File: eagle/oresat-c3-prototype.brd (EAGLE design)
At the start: 99.8 x 94.7 mm, 106 parts, among them J1 J-SAMTEC-TFM-110-X1-XXX-D-RA, J2 U.FL, J3 U.FL, J4 U.FL, J6 J-SAMTEC-TFM-120-X1-XXX-D-RA, J7 FTSH-105-XX-X-DV-K, J8 SD_CARD_SOCKET, Q1 MOSFET-PCH-SOT23-6, Q3 MOSFET-PCH-SOT23-6, Q4 MOSFET-PCH-SOT23-6, Q5 PMV45EN, Q6 PMV45EN, U1 MAX4211CETE, U2 TCAN330, U3 TCAN330, U4 MAX4211CETE, U5 TPS62111RSA, U6 MAX6374KA+21-0078H-L, X1 16MHZ-2.5x2mm

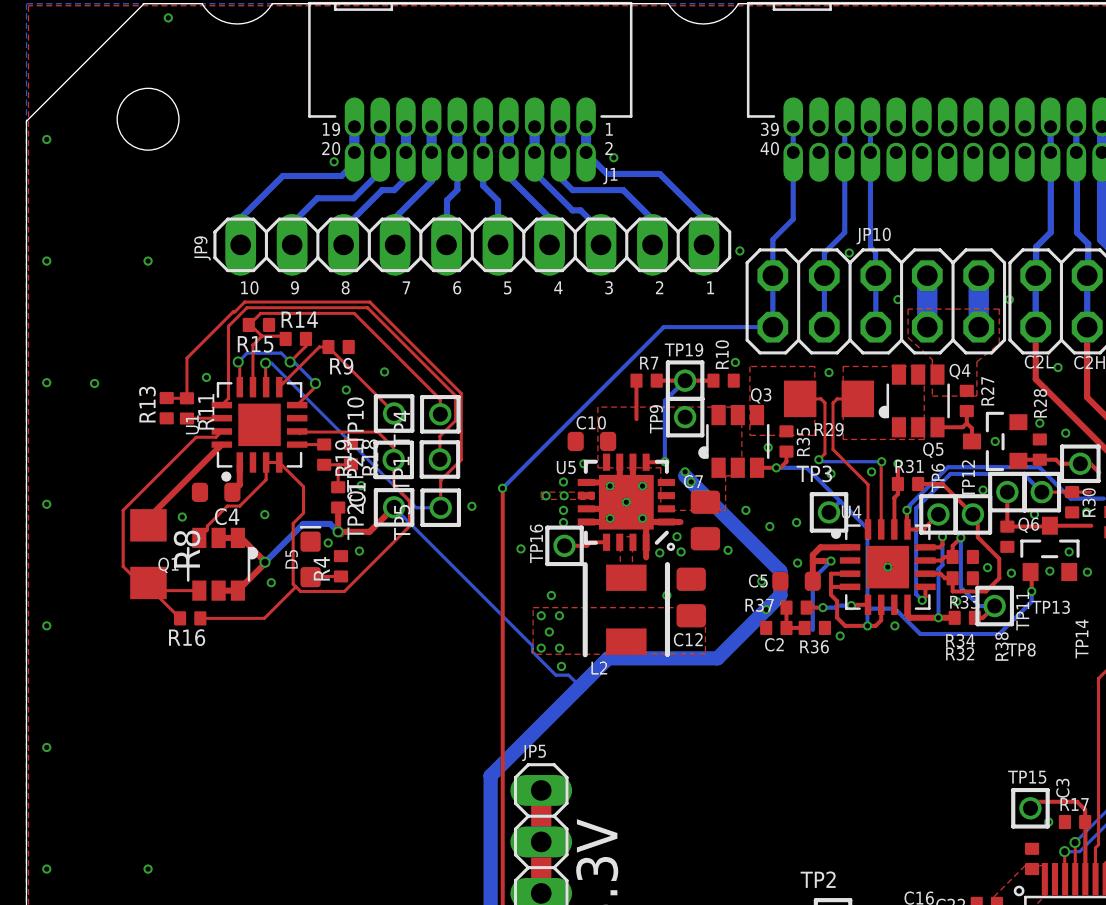
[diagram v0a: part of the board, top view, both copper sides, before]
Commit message: Added the circuit breaker schematic and wired it to the board part tps25961
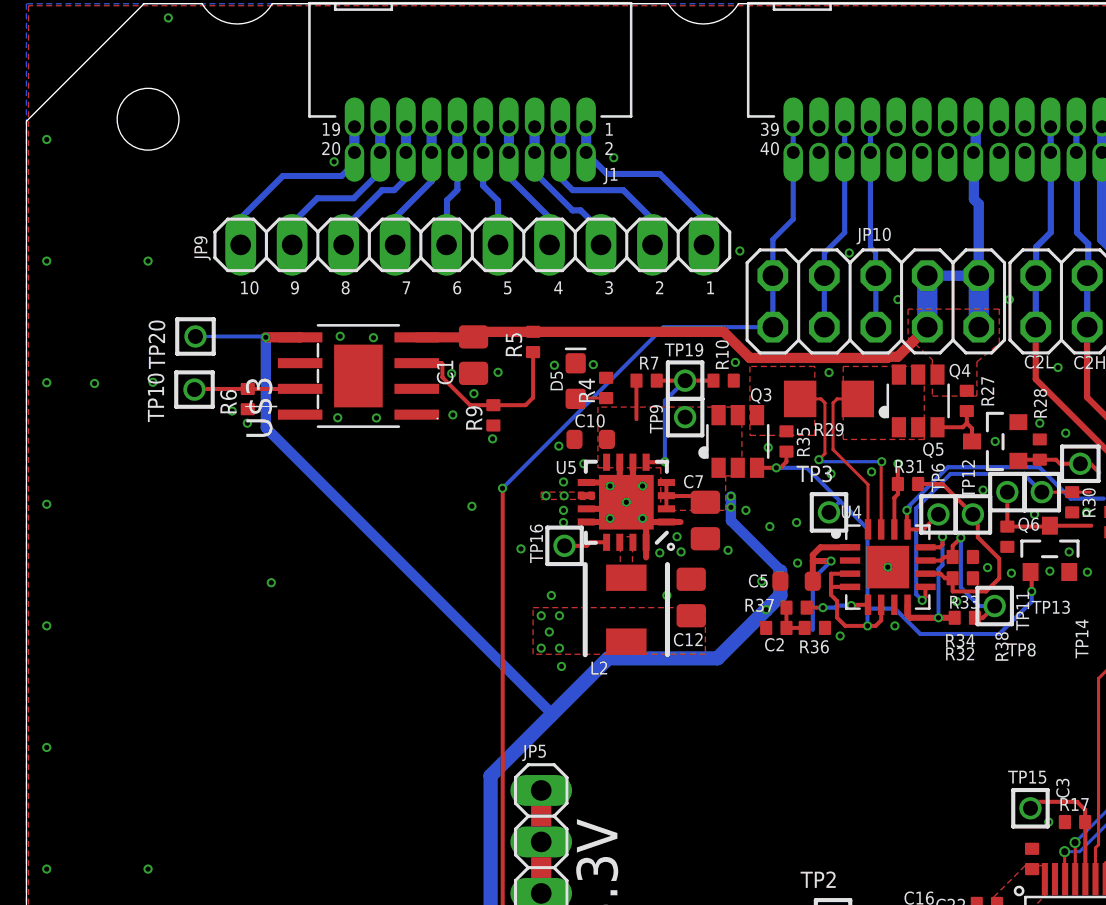
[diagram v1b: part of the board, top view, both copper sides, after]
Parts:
- removed C4: 1u, oresat-rcl:.0603-B-NOSILK
- removed Q1: MOSFET-PCH-SOT23-6, Q-MOSFET-PCH-SOT23-6:SOT23-6
- removed R11, R14: 0, rcl_custom:.0402-B-NOSILK
- removed R13, R15, R18, R19: NP, rcl_custom:.0402-B-NOSILK
- removed R16: 10k, rcl_custom:.0402-B-NOSILK
- removed R8: 100m, rcl:R1206
- removed TP1, TP21, TP4, TP5: TEST-POINT, Tova:2MM-TEST-POINT
- removed U1: MAX4211CETE, U-Maxim-MAX4211-power-monitor:QFN65P400X400X80-17T210
- added R5: 10k, rcl_custom:.0402-B-NOSILK
- added R6: 4.7k, rcl_custom:.0402-B-NOSILK
- added U$3: TI-TPS259621-eFuse, Robins_Parts:SO-POWERPAD-8
- C1: value NP -> 1u; device rcl_custom:.0402-B-NOSILK -> oresat-rcl:.0805-B-NOSILK
- moved D5 15.8 mm to (27.1, 76.1)
- moved R4 15.8 mm to (28.6, 75.7)
- moved TP20 12.9 mm to (8.34, 78.3)
- moved TP10 9.92 mm to (8.29, 75.7)
- moved C1 9.69 mm to (22.1, 77.4), turned to 90 degrees
- moved R9 8.35 mm to (23.0, 74.4), turned to 90 degrees
- moved C10 0.12 mm to (27.8, 73.2)
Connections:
- removed net CB_POUT: TP1.1, U1.13
- removed net IOUT1: R11.2, U1.14
- removed net N$402: R9.2, TP10.1, U1.9
- removed net N$403: R11.1, R13.2, TP5.1, U1.10
- removed net N$404: R14.1, R15.2, TP4.1, U1.11
- removed net N$405: R14.2, U1.12, U1.8
- removed net N$407: R19.1, U1.5
- removed net N$479: C1.1, R18.2, R19.2
- removed net N$480: Q1.4, R16.2, R8.2, U1.15
- new net EN/UVLO: R5.1, R9.2, U$3.3
- new net ILIM: R6.2, TP10.1, U$3.7
- net 3.3V: no longer C4.1, U1.1
- net CB_CTRL: no longer Q1.3, R16.1, TP21.1, U1.3, U1.4, U1.6
- net GND: now also C1.1, R6.1, U$3.1, U$3.THERMAL; no longer C4.2, R13.1, R15.1, R18.1, U1.7, U1.EPAD
- net VBUS: now also C1.2, R5.2, U$3.4; no longer R8.1, U1.16
- net VBUSP: now also U$3.5; no longer C1.2, Q1.1, Q1.2, Q1.5, Q1.6
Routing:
- net N$403: track 38.4 -> 0.00 mm, vias 1 -> 0
- net CB_CTRL: track 66.4 -> 31.6 mm
- net VBUS: track 10.6 -> 41.6 mm
- net CB_POUT: track 20.9 -> 0.00 mm
- net N$404: track 17.4 -> 0.00 mm
- net N$480: track 15.5 -> 0.00 mm
- net EN/UVLO: track 0.00 -> 9.40 mm
- net N$405: track 9.04 -> 0.00 mm, vias 3 -> 0
- net N$402: track 7.87 -> 0.00 mm
- net ILIM: track 0.00 -> 5.19 mm
- net N$479: track 2.44 -> 0.00 mm
- net VBUSP: track 100.1 -> 102.5 mm, vias 5 -> 4
- net IOUT1: track 1.73 -> 0.00 mm
- net 3.3V: track 109.7 -> 108.1 mm
- net N$407: track 1.33 -> 0.00 mm
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
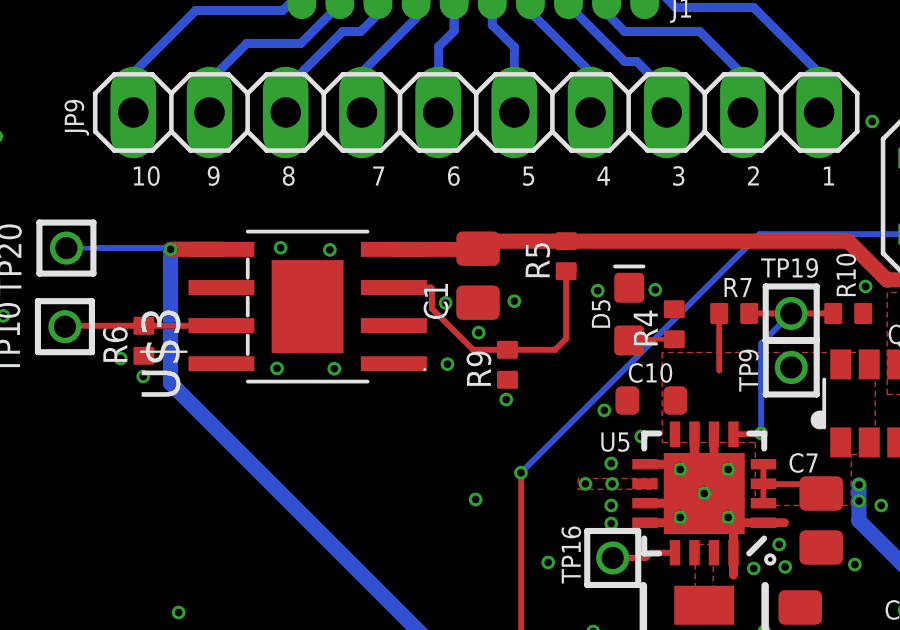
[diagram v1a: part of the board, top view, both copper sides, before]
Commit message: I corrected R_ILIM on the CB to set the over current limit to 0.302 A.
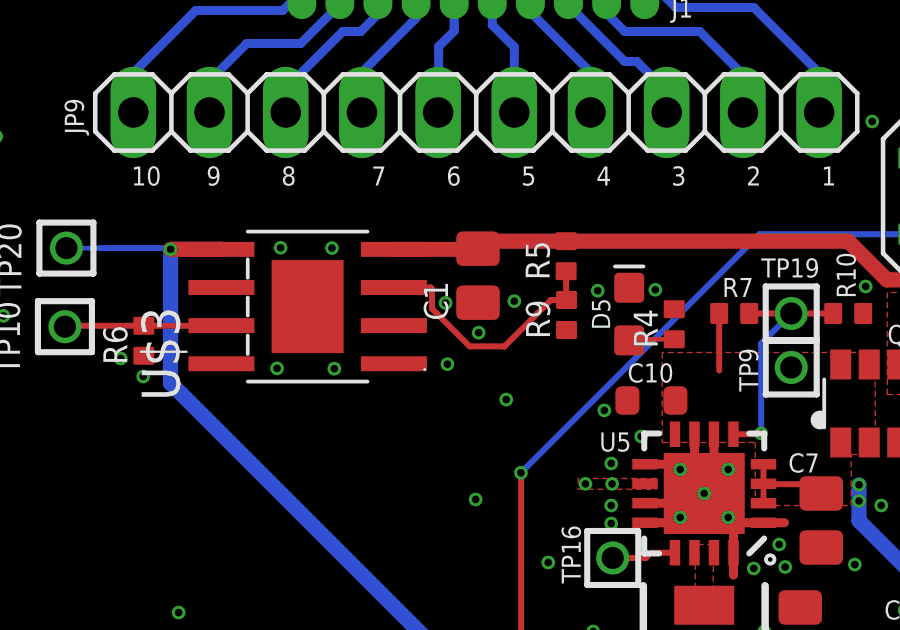
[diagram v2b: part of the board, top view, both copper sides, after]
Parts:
- R6: value 4.7k -> 3.1k
- moved R9 2.58 mm to (25.0, 76.0)
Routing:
- net EN/UVLO: track 9.40 -> 8.57 mm
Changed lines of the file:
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@@
 <attribute name="VALUE" x="29.95" y="74.94" size="0.8" layer="27" font="vector" ratio="15" rot="R90"/>
 </element>
-<element name="R9" library="rcl_custom" package=".0402-B-NOSILK" value="10k" x="23.04" y="74.39" smashed="yes" rot="R90">
-<attribute name="DIS" value="Digi-Key" x="17.74" y="68.49" size="1.778" layer="27" rot="R90" display="off"/>
-<attribute name="DPN" value="1276-4275-1-ND" x="17.74" y="68.49" size="1.778" layer="27" rot="R90" display="off"/>
-<attribute name="MFR" value="Samsung" x="17.74" y="68.49" size="1.778" layer="27" rot="R90" display="off"/>
-<attribute name="MPN" value="RC1005F6653CS" x="17.74" y="68.49" size="1.778" layer="27" rot="R90" display="off"/>
-<attribute name="NAME" x="22.49" y="73.59" size="0.8" layer="25" font="vector" ratio="15" rot="R90"/>
-<attribute name="NAME" x="23.04" y="74.39" size="0.2" layer="33" ratio="15" rot="R90" align="center"/>
-<attribute name="VALUE" x="24.39" y="73.59" size="0.8" layer="27" font="vector" ratio="15" rot="R90"/>
+<element name="R9" library="rcl_custom" package=".0402-B-NOSILK" value="10k" x="25.01" y="76.05" smashed="yes" rot="R90">
+<attribute name="DIS" value="Digi-Key" x="19.71" y="70.15" size="1.778" layer="27" rot="R90" display="off"/>
+<attribute name="DPN" value="1276-4275-1-ND" x="19.71" y="70.15" size="1.778" layer="27" rot="R90" display="off"/>
+<attribute name="MFR" value="Samsung" x="19.71" y="70.15" size="1.778" layer="27" rot="R90" display="off"/>
+<attribute name="MPN" value="RC1005F6653CS" x="19.71" y="70.15" size="1.778" layer="27" rot="R90" display="off"/>
+<attribute name="NAME" x="24.46" y="75.25" size="0.8" layer="25" font="vector" ratio="15" rot="R90"/>
+<attribute name="NAME" x="25.01" y="76.05" size="0.2" layer="33" ratio="15" rot="R90" align="center"/>
+<attribute name="VALUE" x="26.36" y="75.25" size="0.8" layer="27" font="vector" ratio="15" rot="R90"/>
 </element>
 <element name="TP10" library="Tova" package="2MM-TEST-POINT" value="TEST-POINT" x="8.29" y="75.66" smashed="yes" rot="R90">
@@
 <attribute name="VALUE" x="23.86" y="75.86" size="0.8" layer="27" font="vector" ratio="15" rot="R90"/>
 </element>
-<element name="R6" library="rcl_custom" package=".0402-B-NOSILK" value="4.7k" x="10.92" y="75.19" smashed="yes" rot="R90">
+<element name="R6" library="rcl_custom" package=".0402-B-NOSILK" value="3.1k" x="10.92" y="75.19" smashed="yes" rot="R90">
 <attribute name="DIS" value="Digi-Key" x="10.92" y="75.19" size="1.778" layer="27" rot="R90" display="off"/>
 <attribute name="DPN" value="1276-4275-1-ND" x="10.92" y="75.19" size="1.778" layer="27" rot="R90" display="off"/>
@@
 <via x="17.27" y="74.26" extent="1-16" drill="0.254"/>
 <via x="15.48" y="78.29" extent="1-16" drill="0.254"/>
-<via x="17.12" y="78.22" extent="1-16" drill="0.254"/>
+<via x="17.19" y="78.28" extent="1-16" drill="0.254"/>
 <wire x1="98.8" y1="88" x2="93" y2="94" width="0" layer="19" extent="1-1"/>
 <wire x1="98.8" y1="82" x2="98.8" y2="88" width="0" layer="19" extent="1-1"/>
@@
 <wire x1="36.6" y1="72.8" x2="35.5" y2="69.7" width="0" layer="19" extent="1-1"/>
 <wire x1="23" y1="73.23" x2="26.27" y2="72.87" width="0" layer="19" extent="1-1"/>
-<wire x1="23.04" y1="73.89" x2="23" y2="73.23" width="0" layer="19" extent="1-1"/>
-<wire x1="22.08" y1="75.46" x2="23.04" y2="73.89" width="0" layer="19" extent="1-1"/>
+<wire x1="25.01" y1="75.55" x2="23" y2="73.23" width="0" layer="19" extent="1-1"/>
+<wire x1="22.08" y1="75.46" x2="25.01" y2="75.55" width="0" layer="19" extent="1-1"/>
 <wire x1="22.06" y1="76.46" x2="22.08" y2="75.46" width="0" layer="19" extent="1-1"/>
 <wire x1="20.98" y1="76.45" x2="22.06" y2="76.46" width="0" layer="19" extent="1-1"/>
@@
 <wire x1="15.36" y1="74.27" x2="17.27" y2="74.26" width="0" layer="19" extent="1-1"/>
 <wire x1="16.38" y1="76.33" x2="17.27" y2="74.26" width="0" layer="19" extent="1-1"/>
-<wire x1="17.12" y1="78.22" x2="16.38" y2="76.33" width="0" layer="19" extent="1-1"/>
-<wire x1="15.48" y1="78.29" x2="17.12" y2="78.22" width="0" layer="19" extent="1-1"/>
+<wire x1="17.19" y1="78.28" x2="16.38" y2="76.33" width="0" layer="19" extent="1-1"/>
+<wire x1="15.48" y1="78.29" x2="17.19" y2="78.28" width="0" layer="19" extent="1-1"/>
 <wire x1="26.05" y1="76.86" x2="23.27" y2="76.51" width="0" layer="19" extent="1-1"/>
 <wire x1="27.1" y1="76.957" x2="26.05" y2="76.86" width="0" layer="19" extent="1-1"/>
@@
 <contactref element="R5" pad="1"/>
 <contactref element="U$3" pad="3"/>
-<wire x1="20.5244" y1="76.26128125" x2="20.5244" y2="76.9256" width="0.2" layer="1"/>
-<wire x1="23.04" y1="74.89" x2="21.89568125" y2="74.89" width="0.2" layer="1"/>
-<wire x1="21.89568125" y1="74.89" x2="20.5244" y2="76.26128125" width="0.2" layer="1"/>
-<wire x1="20.485" y1="76.965" x2="19.255" y2="76.965" width="0.2" layer="1"/>
-<wire x1="20.5244" y1="76.9256" x2="20.485" y2="76.965" width="0.2" layer="1"/>
-<wire x1="23.04" y1="74.89" x2="24.63" y2="74.89" width="0.2" layer="1"/>
-<wire x1="24.63" y1="74.89" x2="24.998253125" y2="75.258253125" width="0.2" layer="1"/>
-<wire x1="24.998253125" y1="75.258253125" x2="24.998253125" y2="77.51" width="0.2" layer="1"/>
+<wire x1="24.49" y1="76.55" x2="25.01" y2="76.55" width="0.2" layer="1"/>
+<wire x1="19.255" y1="76.965" x2="20.485" y2="76.965" width="0.2" layer="1"/>
+<wire x1="25.01" y1="76.55" x2="24.998253125" y2="76.55" width="0.2" layer="1"/>
+<wire x1="24.998253125" y1="76.55" x2="24.998253125" y2="77.51" width="0.2" layer="1"/>
+<wire x1="22.9356" y1="75.0044" x2="22.94" y2="75" width="0.2" layer="1"/>
+<wire x1="20.5244" y1="76.26128125" x2="21.78128125" y2="75.0044" width="0.2" layer="1"/>
+<wire x1="21.78128125" y1="75.0044" x2="22.9356" y2="75.0044" width="0.2" layer="1"/>
+<wire x1="20.485" y1="76.965" x2="20.5244" y2="76.9256" width="0.2" layer="1"/>
+<wire x1="20.5244" y1="76.9256" x2="20.5244" y2="76.26128125" width="0.2" layer="1"/>
+<wire x1="22.94" y1="75" x2="24.49" y2="76.55" width="0.2" layer="1"/>
 </signal>
 <signal name="ILIM">

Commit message: layed out most of the board awaiting review and adding BOM
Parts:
- added Q1: MOSFET-PCH-SOT23-6, Q-MOSFET-PCH-SOT23-6:SOT23-6
- added R11, R13, R8: 4.7k, rcl:R0402
- U6: value MAX6374KA+21-0078H-L -> MAX6373KA+21-0078H-L
- moved C9 26.5 mm to (46.6, 44.1), turned to 270 degrees
- moved TP15 2.54 mm to (48.7, 57.4)
- moved R17 1.32 mm to (51.8, 55.6)
- moved C5 0.35 mm to (38.0, 66.5)
- moved U6 0.11 mm to (38.1, 44.0)
- moved R38 0.07 mm to (48.4, 68.5)
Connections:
- removed net SDIO_CK: J8.5, U$2.53
- removed net SDIO_CMD: J8.2, U$2.54
- removed net SDIO_D0: J8.7, U$2.39
- removed net SDIO_D1: J8.8, U$2.40
- removed net SDIO_D2: J8.9, U$2.51
- removed net SDIO_D3: J8.1, U$2.52
- new net MMC_CS: J8.1, U$2.40
- new net N$6: J8.4, Q1.1, Q1.2, Q1.5, Q1.6
- new net SD_PWR_CYC: Q1.3
- new net SPI3_MISO: J8.7, U$2.52
- new net SPI3_MOSI: J8.2, U$2.53
- new net SPI3_SCK: J8.5, U$2.51
- net !SD: now also R13.2
- net 3.3V: now also Q1.4, R11.1, R13.1, R8.1; no longer J8.4
- net OPD_SCL: now also R8.2
- net OPD_SDA: now also R11.2
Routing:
- net 3.3V: track 108.1 -> 203.4 mm, vias 10 -> 15
- net OPD_ON/!OFF: track 4.28 -> 47.7 mm, vias 0 -> 2
- net OPD_PWR: track 10.6 -> 53.7 mm, vias 0 -> 1
- net CAN1_H: track 10.7 -> 48.9 mm
- net CAN1_L: track 10.7 -> 47.2 mm
- net OPD_!FAULT: track 5.86 -> 42.2 mm, vias 0 -> 2
- net OPD_CB_RESET: track 15.1 -> 51.2 mm, vias 1 -> 2
- net OPD_POUT_IN: track 0.00 -> 31.8 mm, vias 0 -> 2
- net SPI3_MOSI: track 0.00 -> 30.7 mm, vias 0 -> 2
- net PA15: track 3.31 -> 34.0 mm, vias 1 -> 2
- net SPI3_MISO: track 0.00 -> 29.3 mm, vias 0 -> 2
- net SPI3_SCK: track 0.00 -> 24.1 mm, vias 0 -> 2
- net MMC_CS: track 0.00 -> 22.6 mm
- net NRST: track 67.0 -> 78.2 mm
- net OPD_SDA: track 39.3 -> 48.4 mm
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
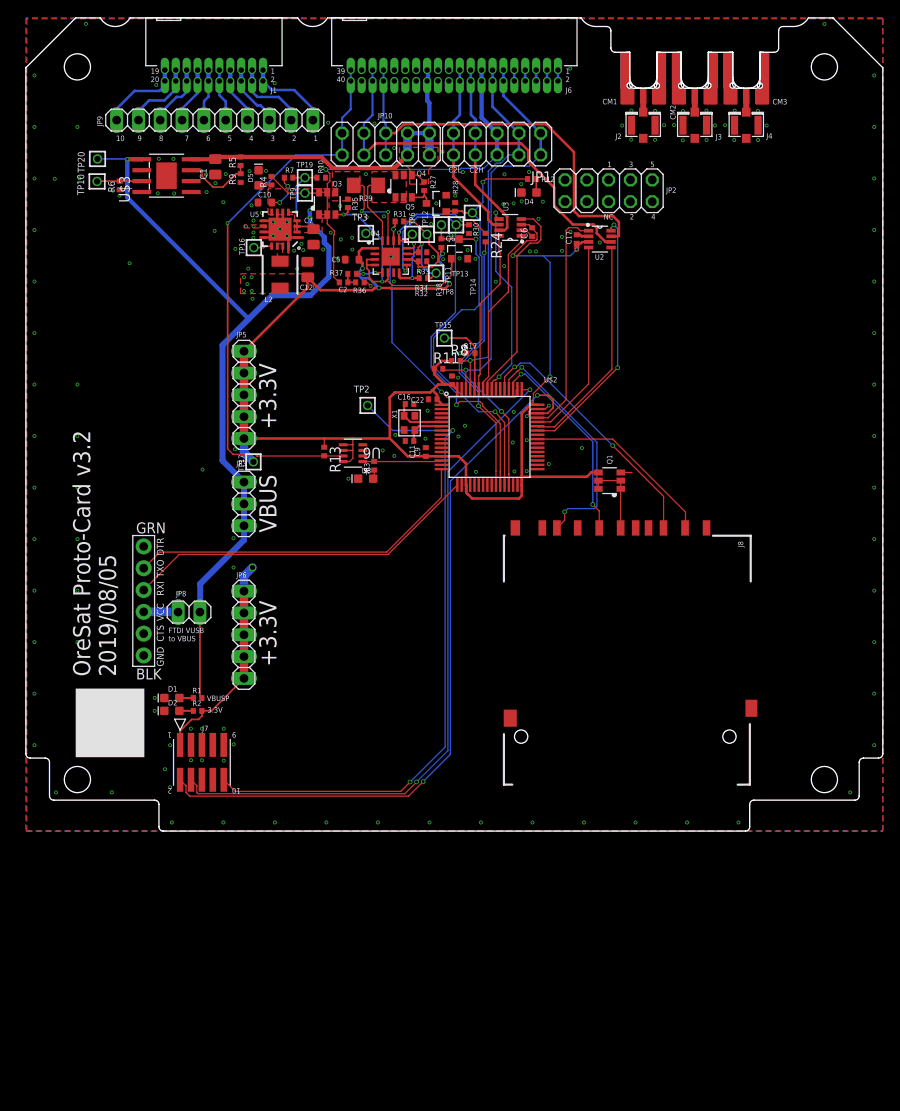
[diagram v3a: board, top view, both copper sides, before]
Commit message: Routed spare pins to header and a little cleanup
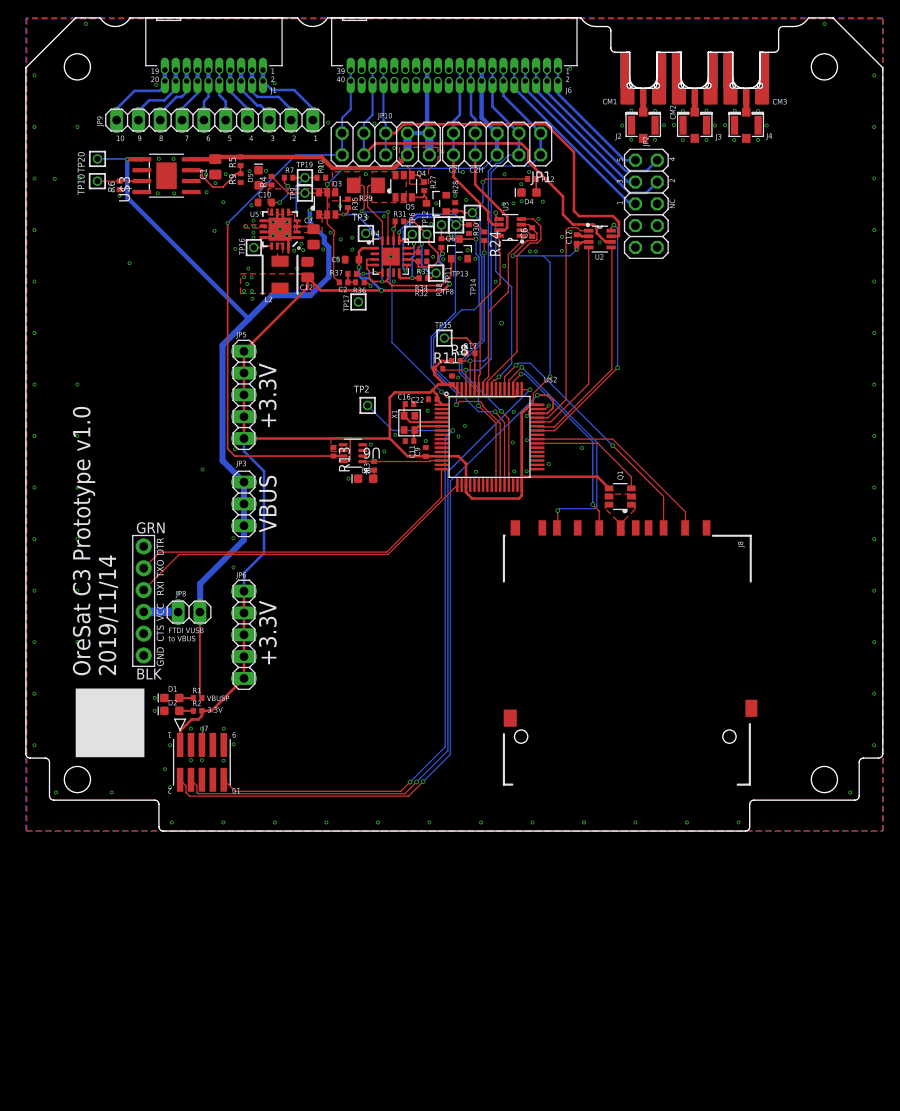
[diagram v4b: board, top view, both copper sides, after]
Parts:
- moved TP17 22.3 mm to (38.7, 61.6)
- moved JP2 4.65 mm to (72.3, 73.0), turned to 270 degrees
- moved Q1 2.23 mm to (69.2, 39.0)
- moved R13 1.07 mm to (35.8, 44.2)
- moved R24 0.22 mm to (53.4, 69.3)
- moved TP10 0.05 mm to (8.33, 75.7)
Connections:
- net N$6 renamed MMC_VDD
- removed net SD_PWR_CYC: Q1.3
- new net MMC_PWR: Q1.3, U$2.39
- net GND: now also JP2.10, JP2.9
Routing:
- net SPARE2: track 1.27 -> 23.1 mm
- net SPARE1: track 1.27 -> 21.8 mm
- net SPARE4: track 1.27 -> 19.7 mm
- net SPARE3: track 1.56 -> 18.6 mm
- net MMC_PWR: track 0.00 -> 13.9 mm
- net SPARE5: track 1.56 -> 15.3 mm
- net 3.3V: track 203.4 -> 214.9 mm, vias 15 -> 14
- net MMC_VDD: track 9.06 -> 0.01 mm
- net OPD_PWR: track 53.7 -> 52.2 mm
- net SD_PWR_CYC: track 1.32 -> 0.00 mm
- net WDT: track 9.97 -> 9.22 mm
- net SPI3_MISO: track 29.3 -> 29.8 mm
- net GND: vias 192 -> 193
- added copper zone on layer 1, net MMC_VDD
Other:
- board text added: "2019/11/14"
- board text added: "OreSat C3 Prototype v1.0"
- board text removed: "2019/08/05"
- board text removed: "OreSat Proto-Card v3.2"
